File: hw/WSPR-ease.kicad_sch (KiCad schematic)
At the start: 44 parts, among them J101 pwr+data, J102 SMA, J103 SMA, Q101 MMBF170, U101 SRV05-4, U102 ESP32-S3-WROOM-1-N8R8, U103 LMR51430YDDCR, U104 GNSS module

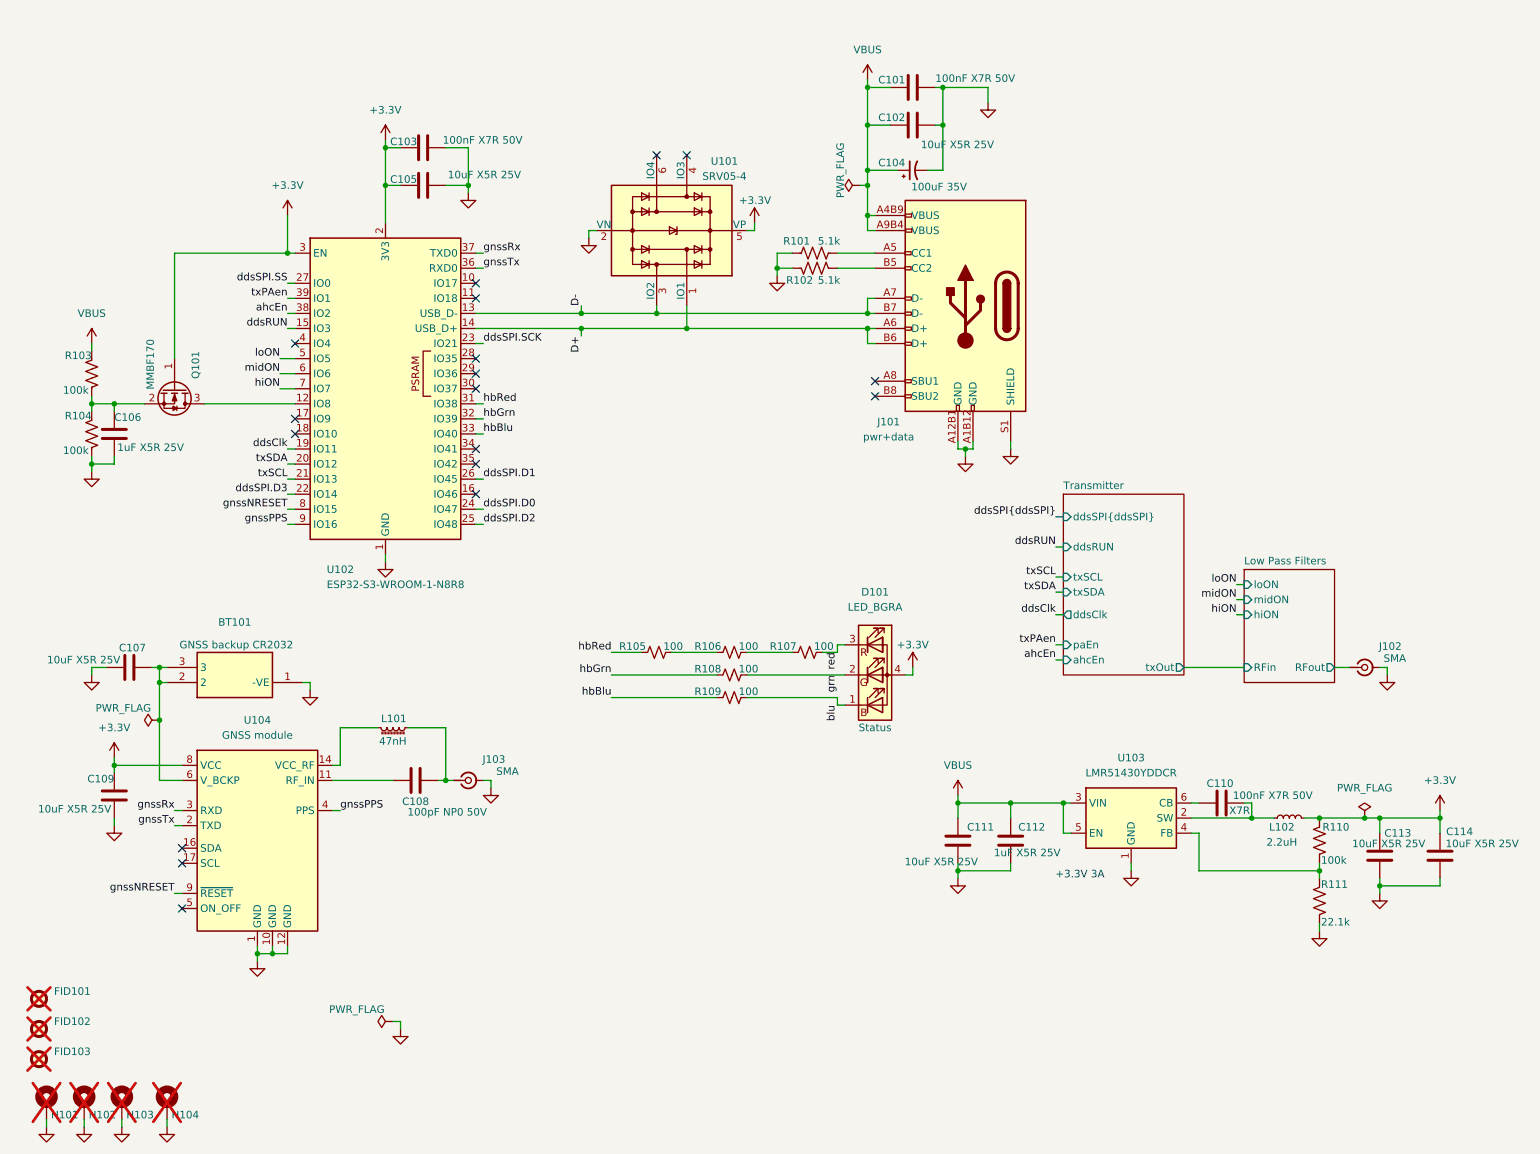
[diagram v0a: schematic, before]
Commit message: Switched to SI5351 clocking MACHXO2 CPLD to drive gate driver for MOSFETs. It passes DRC but needs serious reviewing.
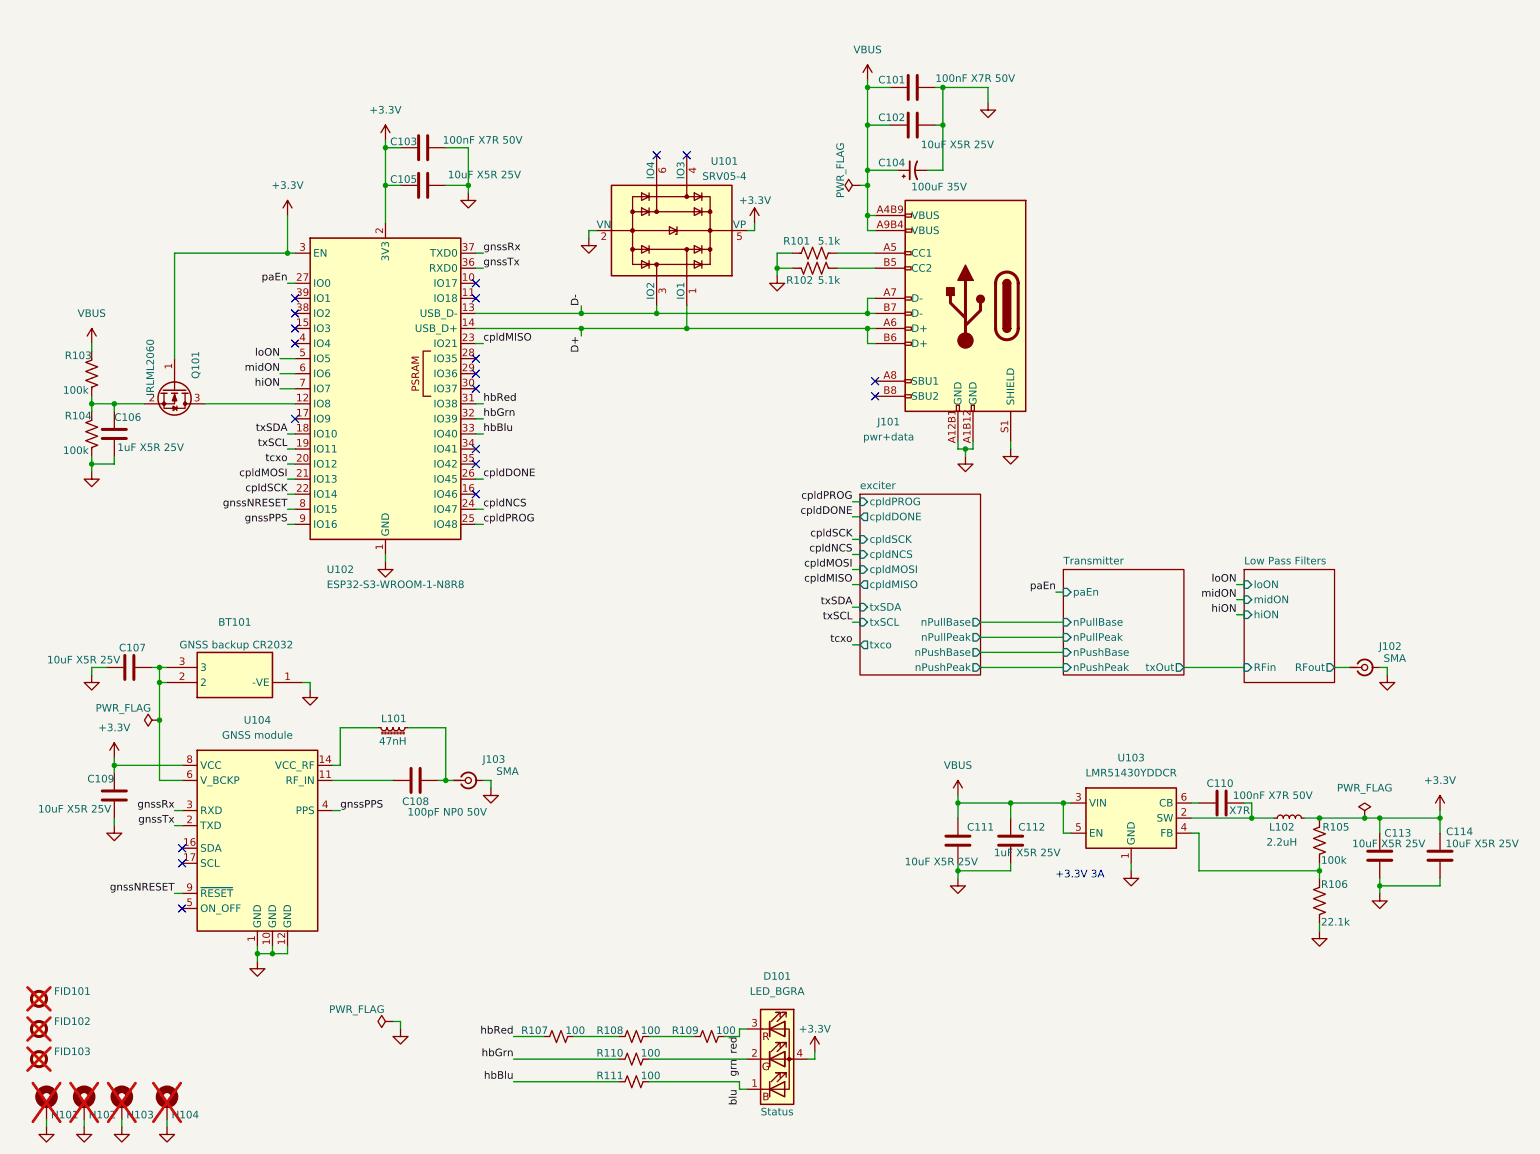
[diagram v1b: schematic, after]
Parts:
- Q101: value MMBF170 -> IRLML2060; LCSC C151058 -> (none); MFG Diodes inc -> Infineon; MPN MMBF170Q-13-F -> IRLML2060TRPBF; Mouser_PN 621-MMBF170Q-13-F -> 942-IRLML2060TRPBF
- renumbered R110 to R105, R111 to R106, R105 to R107, R106 to R108, R107 to R109, R108 to R110, R109 to R111
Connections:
- net ddsClk is gone; now on net txSCL: U102.19 (IO11)
- net txSCL: no longer U102.21 (IO13)
- net txSDA: now also U102.18 (IO10); no longer U102.20 (IO12)
- net ahcEn: no longer names the net of U102.38 (IO2)
- net ddsRUN: no longer names the net of U102.15 (IO3)
- net ddsSPI.D0 renamed cpldNCS
- net ddsSPI.D1 renamed cpldDONE
- net ddsSPI.D2 renamed cpldPROG
- net ddsSPI.D3 renamed cpldSCK
- net ddsSPI.SCK renamed cpldMISO
- net ddsSPI.SS renamed paEn
- net txPAen: no longer names the net of U102.39 (IO1)
- new net cpldMOSI: U102.21 (IO13)
- new net tcxo: U102.20 (IO12)
- no-connect marks 18 -> 20
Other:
- added sheet exciter (exciter.kicad_sch)
- sheet Transmitter ports: added nPullBase, nPullPeak, nPushBase, nPushPeak; removed ahcEn, ddsClk, ddsRUN, ddsSPI{ddsSPI}, txSCL, txSDA
- title: WSPR Ease -> Transmitter
- moved on the sheet: D101, R107, R108, R109, R110, R111

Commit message: Various schematic clean ups. Improved/fixed decoupling around relays. Filter Vdd for TCXO and SI5351 to try to minimize modulation of the clock freq by noise
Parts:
- added C101: 100nF X7R 50V, Capacitor_SMD:C_0402_1005Metric, symbol Device:C
- added TP101: GPIO4, TestPoint:TestPoint_Pad_1.5x1.5mm, symbol Connector:TestPoint
- renumbered C101 to C102, C102 to C103, C103 to C104, C104 to C105, C105 to C106, C106 to C107, C107 to C108, C108 to C109, C109 to C110, C110 to C111, C111 to C112, C112 to C113, C113 to C114, C114 to C115
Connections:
- net GND: now also C101.2
- net VBUS: now also C101.1
- net at U102.4 (IO4): now also TP101.1
- no-connect marks 20 -> 19
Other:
- moved on the sheet: C102, C103

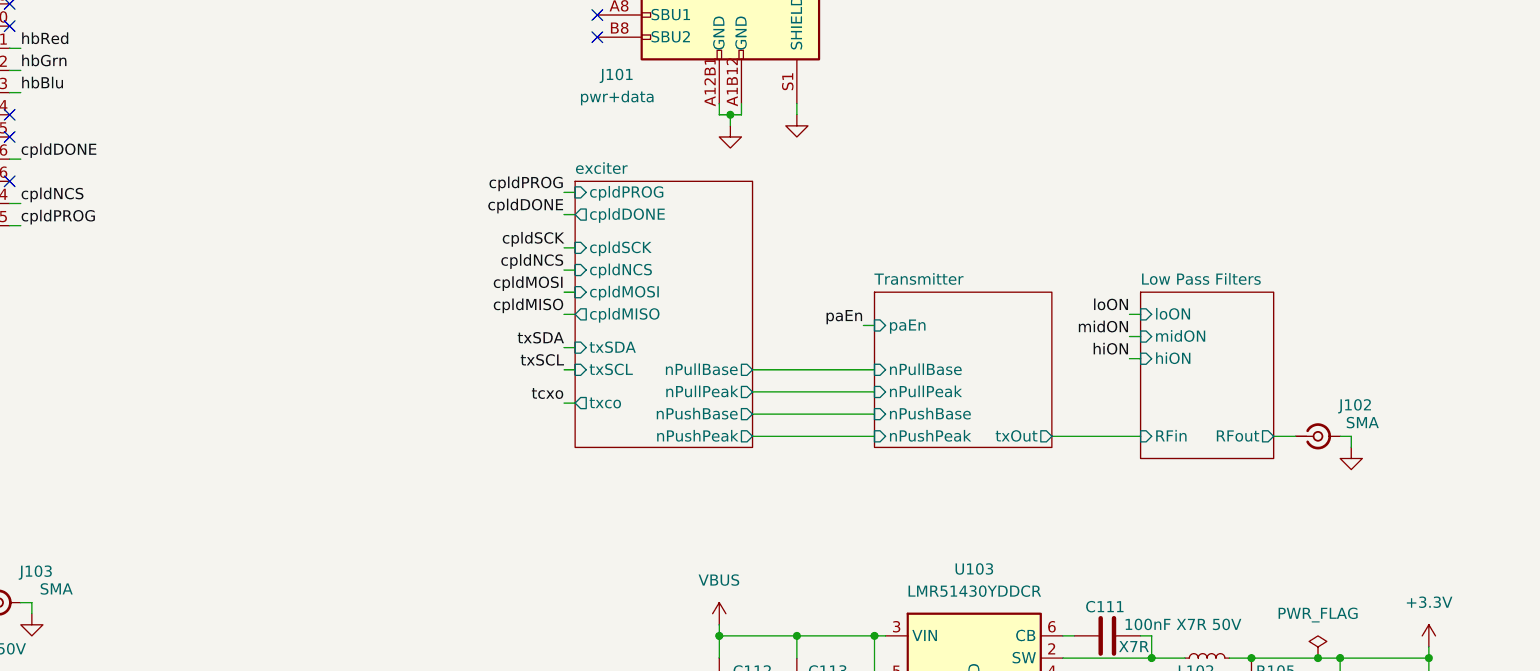
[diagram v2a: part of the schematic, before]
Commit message: Simplify. Put exciter stuff onto transmitter sheet.
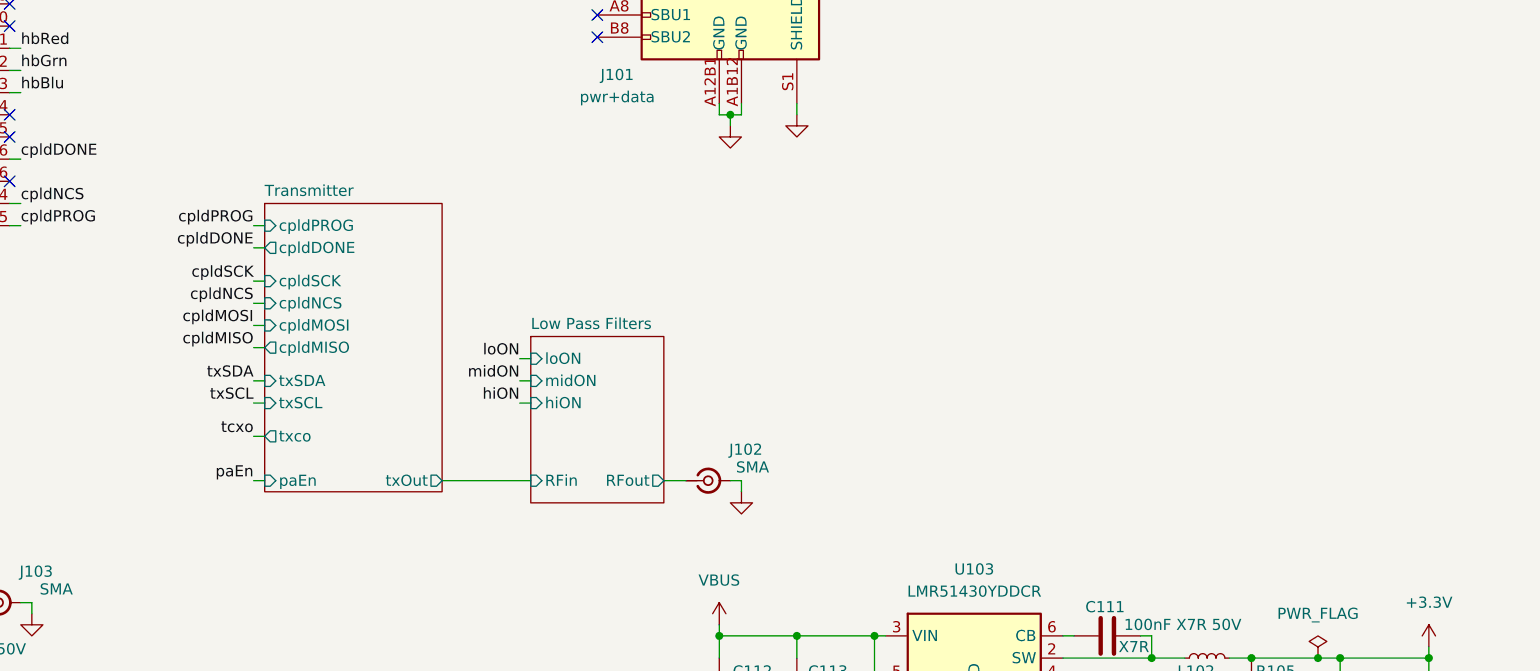
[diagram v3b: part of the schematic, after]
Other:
- removed sheet exciter
- sheet Transmitter ports: added cpldDONE, cpldMISO, cpldMOSI, cpldNCS, cpldPROG, cpldSCK, txSCL, txSDA, txco; removed nPullBase, nPullPeak, nPushBase, nPushPeak
- title: Transmitter -> WSPR-Ease
- moved on the sheet: J102
